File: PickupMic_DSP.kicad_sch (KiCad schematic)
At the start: 0 parts

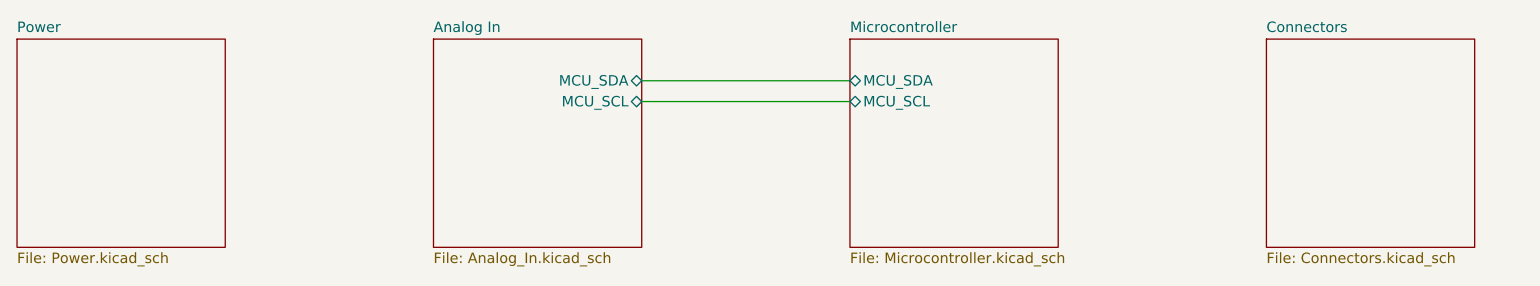
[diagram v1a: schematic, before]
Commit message: Improvements
Switched ADC to ADC128S.
Upgraded USB to USB-C
Improved Analog front end to work with signals better.
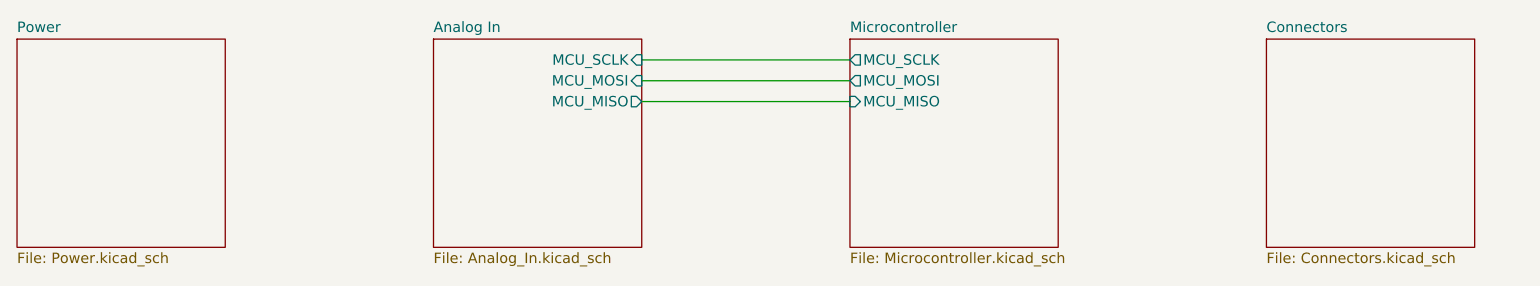
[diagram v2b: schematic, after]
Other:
- sheet Analog In ports: added MCU_MISO, MCU_MOSI, MCU_SCLK; removed MCU_SCL, MCU_SDA
- sheet Microcontroller ports: added MCU_MISO, MCU_MOSI, MCU_SCLK; removed MCU_SCL, MCU_SDA
